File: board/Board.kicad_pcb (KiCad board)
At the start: 2 copper layers, 56 parts, among them J1 CONN_02X10, J10 CONN_01X03, J11 CONN_01X03, J12 CONN_01X02, J13 CONN_02X09, J15 GS3, J16 GS3, J17 GS3, J18 GS2, J19 CONN_01X01, J2 CONN_01X03, J3 CONN_01X03, J4 CONN_01X03, J5 CONN_01X03, J6 CONN_01X03, J7 CONN_01X03, J8 CONN_01X03, J9 CONN_01X03, SW1 SW_Push, U1 STM32F410RBTx, U2 LF33ABDT-TR, U3 ICM-20689, U4 SN74LVC1G04, Y1 25 MHz

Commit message: new pcb
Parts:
- removed J18: GS2, Connect:GS2
- removed J19: CONN_01X01, Pin_Headers:Pin_Header_Straight_1x01_Pitch2.54mm
- removed R10, R11: 10K, Resistors_SMD:R_0805_HandSoldering
- removed R12: 220, Resistors_SMD:R_0805_HandSoldering
- added C13: 0.1uF, Capacitors_SMD:C_0805_HandSoldering, F.Cu at (131.2, 72.7)
- added C14: 100nF, Capacitors_SMD:C_0805_HandSoldering, F.Cu at (213.7, 120.4)
- added C15: 100nF, Capacitors_SMD:C_0805_HandSoldering, F.Cu at (203.8, 135.1)
- added C3: 100nF, Capacitors_SMD:C_0805_HandSoldering, F.Cu at (230.1, 119.7)
- added C4: 100nF, Capacitors_SMD:C_0805_HandSoldering, F.Cu at (224.3, 125.2)
- added C6: 100nF, Capacitors_SMD:C_0805_HandSoldering, F.Cu at (127.0, 86.7)
- added J14: CONN_01X02, Pin_Headers:Pin_Header_Straight_1x02_Pitch2.54mm, F.Cu at (103.1, 73.7)
- added U5: MAG3110, Local_prints:DFN_2x2mm_10pin_0.4pitch, F.Cu at (196.9, 133.7)
- added U6: MS5637, Local_prints:MS5637, F.Cu at (220.7, 109.8)
- C10, C5: value 100nF -> 4.7uF
- C11: value 100nF -> 1uF
- C16: value 4.7uF -> 2.2uF; footprint Capacitors_SMD:C_0805_HandSoldering -> Capacitors_ThroughHole:CP_Radial_D5.0mm_P2.00mm
- C17: value 1uF -> 100nF
- C18: value 100nF -> 10nF
- C19: value 0.1uF -> 1uF
- C20: value 2.2uF -> 0.47uF; footprint Capacitors_ThroughHole:CP_Radial_D5.0mm_P2.00mm -> Capacitors_SMD:C_0805_HandSoldering
- C21: value 10nF -> 100nF
- C22: value 0.47uF -> 2.2uF
- C23: value 2.2uF -> 100nF
- C9: value 4.7uF -> 100nF
- J1: value CONN_02X10 -> GS3; footprint Connect:IDC_Header_Straight_20pins -> Connect:GS3
- J12: value CONN_01X02 -> GS3; footprint Pin_Headers:Pin_Header_Straight_1x02_Pitch2.54mm -> Connect:GS3
- J13: value CONN_02X09 -> GS3; footprint Pin_Headers:Pin_Header_Straight_2x09_Pitch2.54mm -> Connect:GS3
- J15: value GS3 -> CONN_01X03; footprint Connect:GS3 -> Pin_Headers:Pin_Header_Straight_1x03_Pitch2.54mm
- J16: value GS3 -> GS2; footprint Connect:GS3 -> Connect:GS2
- J17: value GS3 -> CONN_01X01; footprint Connect:GS3 -> Pin_Headers:Pin_Header_Straight_1x01_Pitch2.54mm
- J2: value CONN_01X03 -> CONN_02X04; footprint Pin_Headers:Pin_Header_Straight_1x03_Pitch2.54mm -> Pin_Headers:Pin_Header_Straight_2x04_Pitch2.54mm
- R2: value 10K -> 0
- R3: value 0 -> 10K
- R4: value 62K -> 10K
- R5: value 22K -> 10K
- R7: value 10K -> 220
- R8: value 10K -> 62K
- R9: value 10K -> 22K
- U2: value LF33ABDT-TR -> SN74LVC1G04; footprint TO_SOT_Packages_SMD:TO-252-2Lead -> TO_SOT_Packages_SMD:SOT-23-5_HandSoldering
- U3: value ICM-20689 -> LF33ABDT-TR; footprint Housings_DFN_QFN:QFN-24-1EP_4x4mm_Pitch0.5mm -> TO_SOT_Packages_SMD:TO-252-2Lead
- U4: value SN74LVC1G04 -> ICM-20689; footprint TO_SOT_Packages_SMD:SOT-23-5_HandSoldering -> Housings_DFN_QFN:QFN-24-1EP_4x4mm_Pitch0.5mm
- moved D2 134.9 mm to (225.1, 141.5)
- moved R2 118.4 mm to (118.7, 90.3)
- moved U4 112.9 mm to (112.9, 112.0)
- moved C23 110.1 mm to (226.3, 108.6)
- moved C19 110.0 mm to (213.7, 125.9)
- moved C20 109.6 mm to (209.1, 135.1)
- moved C21 108.6 mm to (225.1, 119.7)
- moved U2 102.4 mm to (199.3, 121.5)
- moved C17 92.6 mm to (226.3, 114.1)
- moved J17 91.6 mm to (155.4, 149.0)
- moved C18 90.5 mm to (231.3, 108.6)
- moved J1 89.0 mm to (194.5, 145.1)
- moved C22 86.8 mm to (205.2, 140.6)
- moved C24 80.9 mm to (200.2, 140.6)
- moved J13 62.8 mm to (218.9, 121.8)
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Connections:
- C17 pad 1: VCC -> Net-(C17-Pad1)
- C19 pad 1: +BATT -> VCC
- C20 pad 1: VCC -> Net-(C20-Pad1)
- C22 pad 1: Net-(C22-Pad1) -> VCC
- C5 pad 1: NRST -> Net-(C5-Pad1)
- C9 pad 1: Net-(C9-Pad1) -> VCC
- J1 pad 2: VCC -> Net-(J1-Pad2)
- J1 pad 3: JTRST -> GND
- J10 pad 1: I2C_SCL -> PWM_INPUT_4
- J10 pad 2: I2C_SDA -> Net-(J10-Pad2)
- J11 pad 1: Net-(J11-Pad1) -> I2C_SCL
- J11 pad 2: UART_TX -> I2C_SDA
- J12 pad 1: +BATT -> VCC
- J12 pad 2: GND -> Net-(J12-Pad2)
- J13 pad 1: Net-(J13-Pad1) -> UART_RX
- J13 pad 2: PC8 -> Net-(J13-Pad2)
- J15 pad 1: VCC -> Net-(J13-Pad2)
- J15 pad 2: Net-(J15-Pad2) -> UART_TX
- J16 pad 1: UART_RX -> +BATT
- J16 pad 2: Net-(J11-Pad1) -> Net-(J16-Pad2)
- J17 pad 1: VCC -> Net-(J16-Pad2)
- J2 pad 1: PWM_OUTPUT_1 -> VCC
- J2 pad 2: Net-(J2-Pad2) -> JTCK
- J2 pad 3: GND -> JTRST
- J3 pad 1: PWM_OUTPUT_2 -> PWM_OUTPUT_1
- J4 pad 1: PWM_OUTPUT_3 -> PWM_OUTPUT_2
- J5 pad 1: PWM_OUTPUT_4 -> PWM_OUTPUT_3
- J6 pad 1: PWM_INPUT_1 -> PWM_OUTPUT_4
- J7 pad 1: PWM_INPUT_2 -> PWM_INPUT_1
- J8 pad 1: PWM_INPUT_3 -> PWM_INPUT_2
- J9 pad 1: PWM_INPUT_4 -> PWM_INPUT_3
- R2 pad 1: Net-(J1-Pad11) -> Net-(C1-Pad2)
- R2 pad 2: GND -> Net-(R2-Pad2)
- R3 pad 1: Net-(C1-Pad2) -> Net-(J1-Pad2)
- R4 pad 1: Net-(J18-Pad2) -> VCC
- R4 pad 2: BATT_ADC -> I2C_SCL
- R5 pad 1: BATT_ADC -> VCC
- R5 pad 2: GND -> I2C_SDA
- R6 pad 1: Net-(J1-Pad17) -> Net-(R6-Pad1)
- R6 pad 2: GND -> Net-(J12-Pad2)
- R7 pad 1: Net-(J1-Pad19) -> Net-(D2-Pad1)
- R8 pad 1: Net-(J15-Pad2) -> Net-(J16-Pad2)
- R8 pad 2: Net-(R8-Pad2) -> BATT_ADC
- R9 pad 1: VCC -> BATT_ADC
- R9 pad 2: I2C_SCL -> GND
- SW1 pad 2: NRST -> Net-(C3-Pad1)
- U1 pad 10: PC2 -> Net-(U1-Pad10)
- U1 pad 11: PC3 -> MAG_INT
- U1 pad 2: PC13 -> Net-(U1-Pad2)
- U1 pad 28: Net-(R11-Pad1) -> Net-(R6-Pad1)
- U1 pad 30: Net-(C9-Pad1) -> Net-(C5-Pad1)
- U1 pad 38: PC7 -> Net-(U1-Pad38)
- U1 pad 39: PC8 -> Net-(U1-Pad39)
- U1 pad 40: PC9 -> Net-(U1-Pad40)
- U1 pad 45: PA12 -> Net-(U1-Pad45)
- U1 pad 5: Net-(R3-Pad2) -> Net-(R2-Pad2)
- U1 pad 52: PC11 -> Net-(U1-Pad52)
- U1 pad 53: PC12 -> Net-(U1-Pad53)
- U1 pad 54: PB11 -> Net-(U1-Pad54)
- U1 pad 57: PB5 -> Net-(U1-Pad57)
- U1 pad 60: Net-(R8-Pad2) -> Net-(R3-Pad2)
- U1 pad 7: NRST -> Net-(C3-Pad1)
- U1 pad 9: PC1 -> Net-(U1-Pad9)
- U2 pad 1: +BATT -> (no net)
- U2 pad 2: GND -> UART_RX
- U2 pad 3: VCC -> GND
- U3 pad 1: (no net) -> +BATT
- U3 pad 2: (no net) -> GND
- U3 pad 3: (no net) -> VCC
- U4 pad 2: UART_RX -> (no net)
- U4 pad 3: GND -> (no net)
- U4 pad 4: Net-(J16-Pad3) -> (no net)
- U4 pad 5: VCC -> (no net)

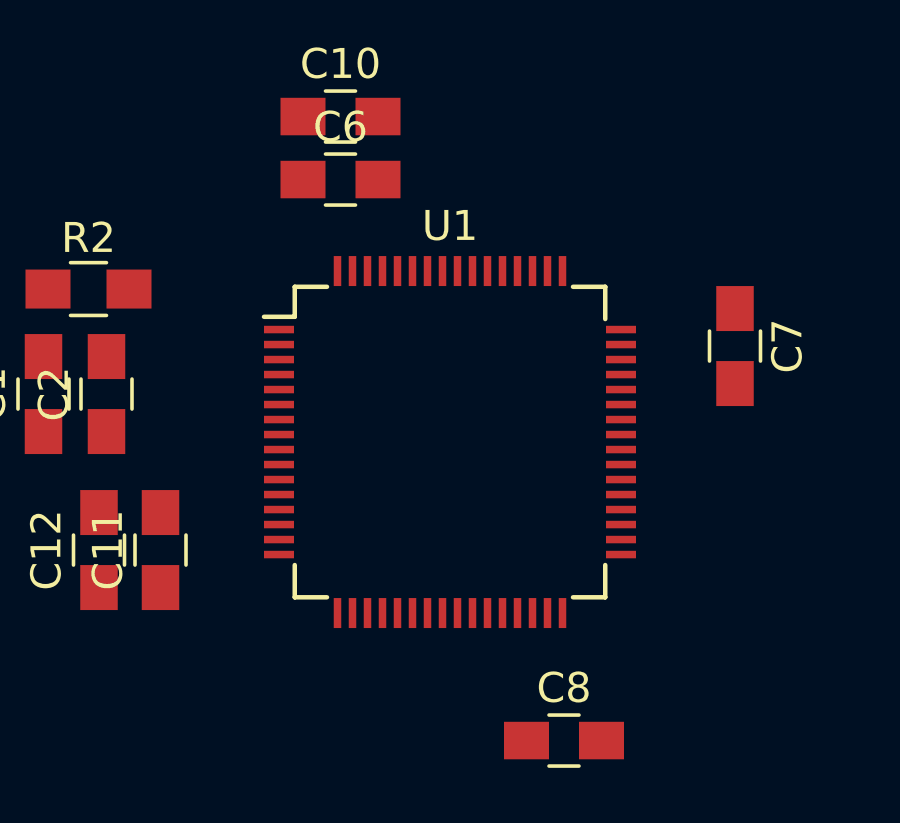
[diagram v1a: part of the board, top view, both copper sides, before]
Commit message: assigned the new footprint
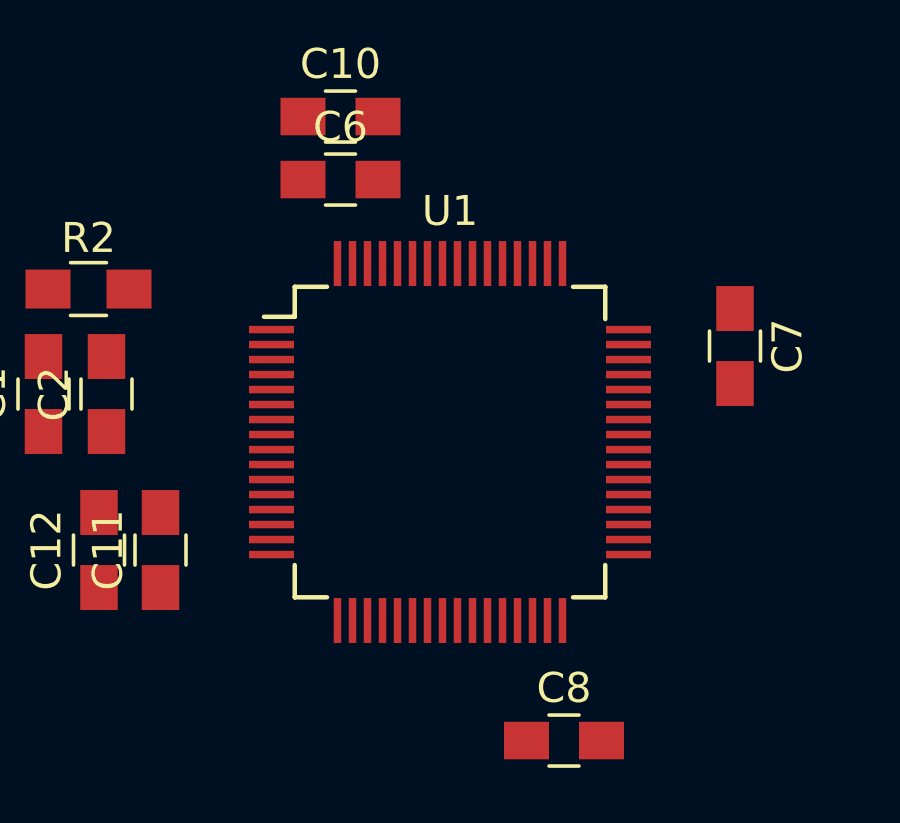
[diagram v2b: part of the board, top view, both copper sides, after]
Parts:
- U1: footprint Housings_QFP:LQFP-64_10x10mm_Pitch0.5mm -> Local_prints:LQFP-64_10x10mm_Pitch0.5mm_handsoldering

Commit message: organized the board a bit
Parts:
- added R10: 10K, Resistors_SMD:R_0805_HandSoldering, F.Cu at (115.9, 138.4)
- added R11: 10K, Resistors_SMD:R_0805_HandSoldering, F.Cu at (116.1, 141.5)
- moved C17 127.4 mm to (104.8, 152.3)
- moved C23 124.1 mm to (109.0, 148.9)
- moved C21 124.1 mm to (106.4, 155.8)
- moved C18 120.6 mm to (111.3, 120.6)
- moved C19 113.0 mm to (103.2, 149.6)
- moved C4 112.0 mm to (118.6, 88.2), turned to 180 degrees
- moved D2 110.5 mm to (138.7, 72.6)
- moved U6 107.4 mm to (121.0, 149.6)
- moved C15 105.6 mm to (100.3, 155.9)
- moved R7 101.0 mm to (146.5, 72.6)
- moved U5 99.0 mm to (99.8, 152.8)
- moved C22 97.9 mm to (108.5, 125.2)
- moved C20 93.2 mm to (117.0, 120.5)
- moved C14 92.2 mm to (125.8, 148.4)
- moved C5 86.6 mm to (132.6, 104.0)
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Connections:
- J11 pad 1: I2C_SCL -> I2C1_SCL
- J11 pad 2: I2C_SDA -> I2C1_SDA
- R4 pad 2: I2C_SCL -> I2C1_SCL
- R5 pad 2: I2C_SDA -> I2C1_SDA
- U1 pad 29: Net-(U1-Pad29) -> I2C2_SCL
- U1 pad 54: Net-(U1-Pad54) -> I2C2_SDA
- U1 pad 61: I2C_SCL -> I2C1_SCL
- U1 pad 62: I2C_SDA -> I2C1_SDA
- U5 pad 6: I2C_SDA -> I2C2_SDA
- U5 pad 7: I2C_SCL -> I2C2_SCL
- U6 pad 2: I2C_SDA -> I2C2_SDA
- U6 pad 3: I2C_SCL -> I2C2_SCL

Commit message: a bit more order
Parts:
- moved J10 41.7 mm to (146.7, 87.2), turned to 90 degrees
- moved J2 41.1 mm to (130.5, 77.7), turned to 90 degrees
- moved J6 40.3 mm to (146.7, 103.8), turned to 90 degrees
- moved J9 36.0 mm to (146.7, 83.7), turned to 90 degrees
- moved J5 35.6 mm to (146.7, 100.2), turned to 90 degrees
- moved R7 32.1 mm to (115.8, 82.0)
- moved J8 32.0 mm to (146.7, 80.0), turned to 90 degrees
- moved J4 31.3 mm to (146.7, 96.7), turned to 90 degrees
- moved D2 29.0 mm to (111.2, 82.0), turned to 180 degrees
- moved J7 28.7 mm to (146.7, 76.5), turned to 90 degrees
- moved J3 27.6 mm to (146.7, 93.0), turned to 90 degrees
- moved C17 23.3 mm to (112.6, 130.3)
- moved C19 23.3 mm to (111.0, 127.6)
- moved C14 23.3 mm to (133.6, 126.4)
- moved C23 23.3 mm to (116.8, 127.0)
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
